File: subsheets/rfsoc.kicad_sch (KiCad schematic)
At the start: 29 parts, among them J1 Conn_01x05, U2 ADXL367BCCZ-RL7, U3 nRF54L15-QFXX, X1 32.768 kHz, X2 32MHz

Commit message: Initial RF layout
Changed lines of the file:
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@@
 	(wire
 		(pts
-			(xy 27.94 25.4) (xy 29.21 25.4)
+			(xy 54.61 40.64) (xy 55.88 40.64)
 		)
 		(stroke
@@
 	(wire
 		(pts
-			(xy 29.21 25.4) (xy 29.21 24.13)
+			(xy 55.88 40.64) (xy 55.88 39.37)
 		)
 		(stroke
@@
 	(text "nRF Schematic From: https://docs.nordicsemi.com/bundle/ps_nrf54L15/page/chapters/ref_circuitry.html"
 		(exclude_from_sim no)
-		(at 231.902 14.224 0)
+		(at 231.902 7.62 0)
 		(effects
 			(font
@@
 	(hierarchical_label "LTC_PWR"
 		(shape input)
-		(at 27.94 25.4 180)
+		(at 54.61 40.64 180)
 		(fields_autoplaced yes)
 		(effects
@@
 	(symbol
 		(lib_id "power:VDD")
-		(at 29.21 24.13 0)
+		(at 55.88 39.37 0)
 		(unit 1)
 		(exclude_from_sim no)
@@
 		(fields_autoplaced yes)
 		(property "Reference" "#PWR02"
-			(at 29.21 27.94 0)
+			(at 55.88 43.18 0)
 			(effects
 				(font
@@
 		)
 		(property "Value" "VDD"
-			(at 29.21 19.05 0)
+			(at 55.88 34.29 0)
 			(effects
 				(font
@@
 		)
 		(property "Footprint" ""
-			(at 29.21 24.13 0)
+			(at 55.88 39.37 0)
 			(effects
 				(font
@@
 		)
 		(property "Datasheet" ""
-			(at 29.21 24.13 0)
+			(at 55.88 39.37 0)
 			(effects
 				(font
@@
 		)
 		(property "Description" "Power symbol creates a global label with name \"VDD\""
-			(at 29.21 24.13 0)
-			(effects
-				(font
+			(at 55.88 39.37 0)
+			(effects
+				(font

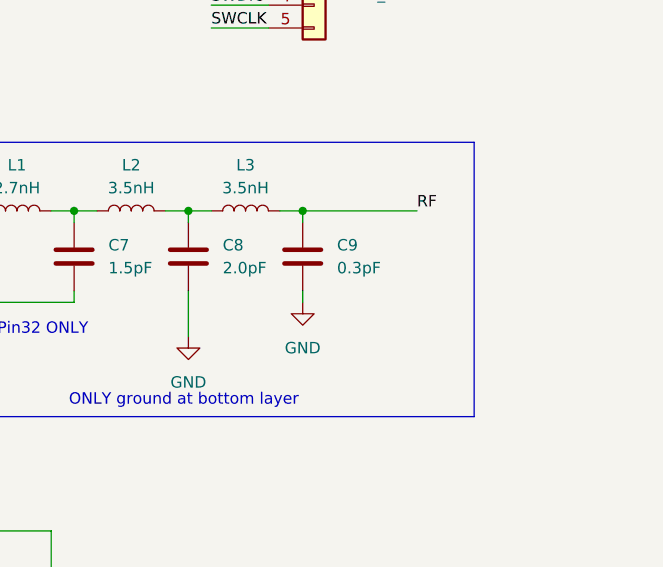
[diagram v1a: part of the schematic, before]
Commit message: Added the rest of the RF stuff
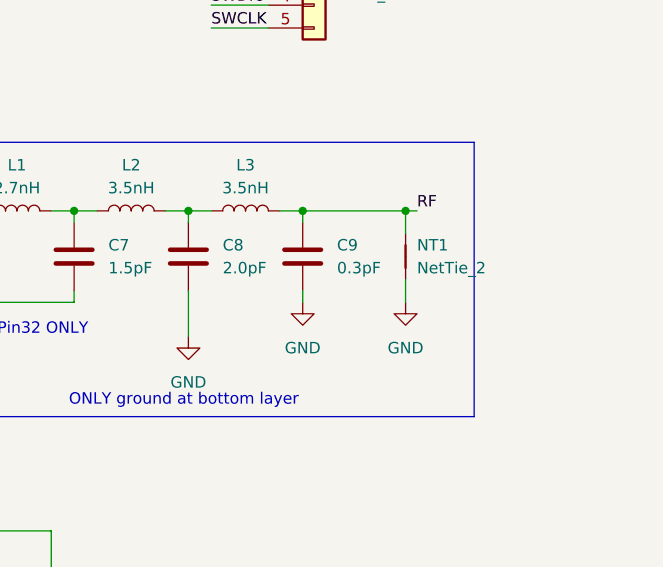
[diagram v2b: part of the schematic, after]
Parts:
- added NT1: NetTie_2, earworm:NetTie-2_SMD_Pad0.33mm, symbol Device:NetTie_2
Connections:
- net GND: now also NT1.1
- net RF: now also NT1.2
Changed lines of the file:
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@@
 	)
 	(junction
+		(at 266.7 80.01)
+		(diameter 0)
+		(color 0 0 0 0)
+	)
+	(junction
 		(at 57.15 106.68)
 		(diameter 0)
@@
 	(wire
 		(pts
-			(xy 255.27 80.01) (xy 267.97 80.01)
+			(xy 255.27 80.01) (xy 266.7 80.01)
 		)
 		(stroke
@@
 	(wire
 		(pts
+			(xy 266.7 87.63) (xy 266.7 90.17)
+		)
+		(stroke
+			(width 0)
+			(type default)
+		)
+	)
+	(wire
+		(pts
 			(xy 128.27 25.4) (xy 128.27 24.13)
 		)
@@
 	(wire
 		(pts
+			(xy 266.7 80.01) (xy 266.7 82.55)
+		)
+		(stroke
+			(width 0)
+			(type default)
+		)
+	)
+	(wire
+		(pts
 			(xy 242.57 52.07) (xy 242.57 49.53)
 		)
@@
 	(wire
 		(pts
+			(xy 266.7 80.01) (xy 267.97 80.01)
+		)
+		(stroke
+			(width 0)
+			(type default)
+		)
+	)
+	(wire
+		(pts
 			(xy 210.82 54.61) (xy 210.82 55.88)
 		)
@@
 	)
 	(symbol
+		(lib_id "Device:NetTie_2")
+		(at 266.7 85.09 90)
+		(unit 1)
+		(exclude_from_sim no)
+		(in_bom no)
+		(on_board yes)
+		(dnp no)
+		(fields_autoplaced yes)
+		(property "Reference" "NT1"
+			(at 267.97 83.8199 90)
+			(effects
+				(font
+					(size 1.27 1.27)
+				)
+				(justify right)
+			)
+		)
+		(property "Value" "NetTie_2"
+			(at 267.97 86.3599 90)
+			(effects
+				(font
+					(size 1.27 1.27)
+				)
+				(justify right)
+			)
+		)
+		(property "Footprint" "earworm:NetTie-2_SMD_Pad0.33mm"
+			(at 266.7 85.09 0)
+			(effects
+				(font
+					(size 1.27 1.27)
+				)
+				(hide yes)
+			)
+		)
+		(property "Datasheet" "~"
+			(at 266.7 85.09 0)
+			(effects
+				(font
+					(size 1.27 1.27)
+				)
+				(hide yes)
+			)
+		)
+		(property "Description" "Net tie, 2 pins"
+			(at 266.7 85.09 0)
+			(effects
+				(font
+					(size 1.27 1.27)
+				)
+				(hide yes)
+			)
+		)
+		(pin "2"
+		)
+		(pin "1"
+		)
+		(instances
+			(project ""
+				(path "/881910d0-5a86-41d0-856d-d1bf2648669f/775ed5aa-f2a7-4007-b181-21772bd09852"
+					(reference "NT1")
+					(unit 1)
+				)
+			)
+		)
+	)
+	(symbol
 		(lib_id "power:GND")
 		(at 102.87 55.88 0)
@@
 					(unit 1)
 				)
+			)
+		)
+	)
+	(symbol
+		(lib_id "power:GND")
+		(at 266.7 90.17 0)
+		(unit 1)
+		(exclude_from_sim no)
+		(in_bom yes)
+		(on_board yes)
+		(dnp no)
+		(fields_autoplaced yes)
+		(property "Reference" "#PWR034"
+			(at 266.7 96.52 0)
+			(effects
+				(font
+					(size 1.27 1.27)
+				)
+				(hide yes)
+			)
+		)
+		(property "Value" "GND"
+			(at 266.7 95.25 0)
+			(effects
+				(font
+					(size 1.27 1.27)
+				)
+			)
+		)
+		(property "Footprint" ""
+			(at 266.7 90.17 0)
+			(effects
+				(font
+					(size 1.27 1.27)
+				)
+				(hide yes)
+			)
+		)
+		(property "Datasheet" ""
+			(at 266.7 90.17 0)
+			(effects
+				(font
+					(size 1.27 1.27)
+				)
+				(hide yes)
+			)
+		)
+		(property "Description" "Power symbol creates a global label with name \"GND\" , ground"
+			(at 266.7 90.17 0)
+			(effects
+				(font
+					(size 1.27 1.27)
+				)
+				(hide yes)
+			)
+		)
+		(pin "1"
+		)
+		(instances
+			(project "earworm_hardware"
+				(path "/881910d0-5a86-41d0-856d-d1bf2648669f/775ed5aa-f2a7-4007-b181-21772bd09852"
+					(reference "#PWR034")
+					(unit 1)
+				)

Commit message: changes from board review
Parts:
- added TP1, TP2, TP3: TestPoint, TestPoint:TestPoint_Pad_D1.0mm, symbol Connector:TestPoint
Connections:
- net at U2.3 (MISO/ASEL): now also U3.15 (P2.04); no longer U3.14 (P2.03)
- net at U2.4 (*CS/SCL): now also U3.16 (P2.05); no longer U3.15 (P2.04)
- net at U2.5 (INT1): now also U3.17 (P2.06); no longer U3.16 (P2.05)
- net at U3.4 (P1.03): now also TP1.1
- net at U3.6 (P1.05): now also TP2.1
- net at U3.8 (P1.07): now also TP3.1
- no-connect marks 24 -> 20

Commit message: rev0
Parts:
- added J3: ~, Connector_Coaxial:SMA_Amphenol_132134-10_Vertical, symbol Connector:Conn_Coaxial
- C1, C11, C2, C3: Part CL10B104KB8NNNC -> GCM155R71C104KA55J; Voltage 50V -> 16V
- C10: footprint Capacitor_SMD:C_0402_1005Metric -> Capacitor_SMD:C_0603_1608Metric; ESR (none) -> 7.5
- C12, C16: Part CL10A225KO8NNNC -> GRM155R61E225ME15D; Tolerance 10% -> 20%
- C13: Part CL10B224KO8NNNC -> GCM155R71C224KE02D; Voltage 16V -> 25V
- C14, C15: Part CL10B103KB8NNNC -> GRM155R71E103KA01J
- C4: Part CL10A106KQ8NNNC -> GRM188R61E106MA73D; Tolerance 10% -> 20%; Voltage 6.3V -> 25V
- C5: Voltage 50V -> 16V
- C6: Part CL10C040CB8NNNC -> GJM1555C1H4R0BB01D; Tolerance 6.25% -> 2.5%
- FB1: Part BLM18BA750SN1D -> BLM15BX750SN1D
- FB2: Part BLM18KG121TN1D -> BLM15PX121SN1D
- R1: Part ERJ-3EKF1001V -> ERJ-2RKF1001X
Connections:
- net GND: now also J3.2 (Ext)
- net RF: now also J3.1 (In)
